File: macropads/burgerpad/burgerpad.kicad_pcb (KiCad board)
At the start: 2 copper layers, 1 part, among them U1 RP2040-ZERO

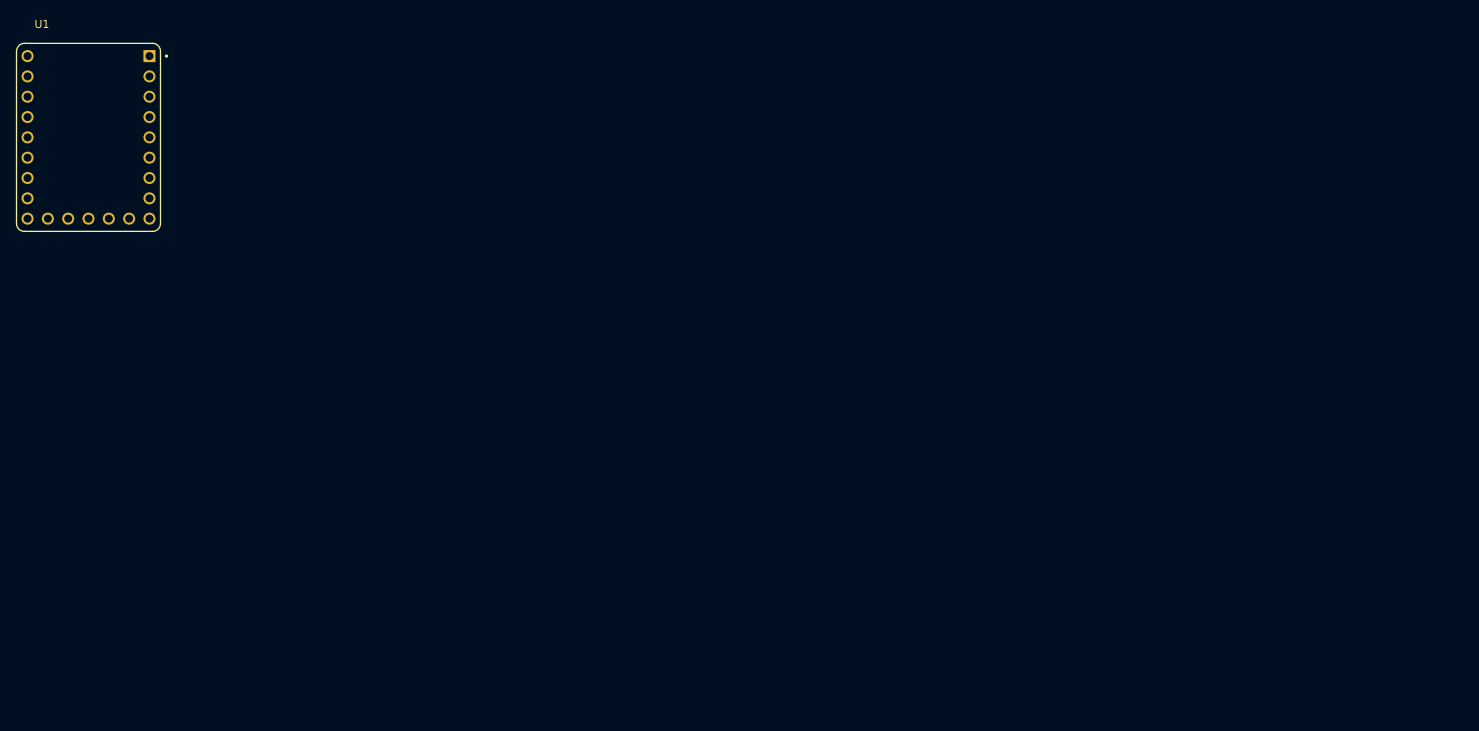
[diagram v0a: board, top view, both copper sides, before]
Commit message: Made schematic and did PCB layouts
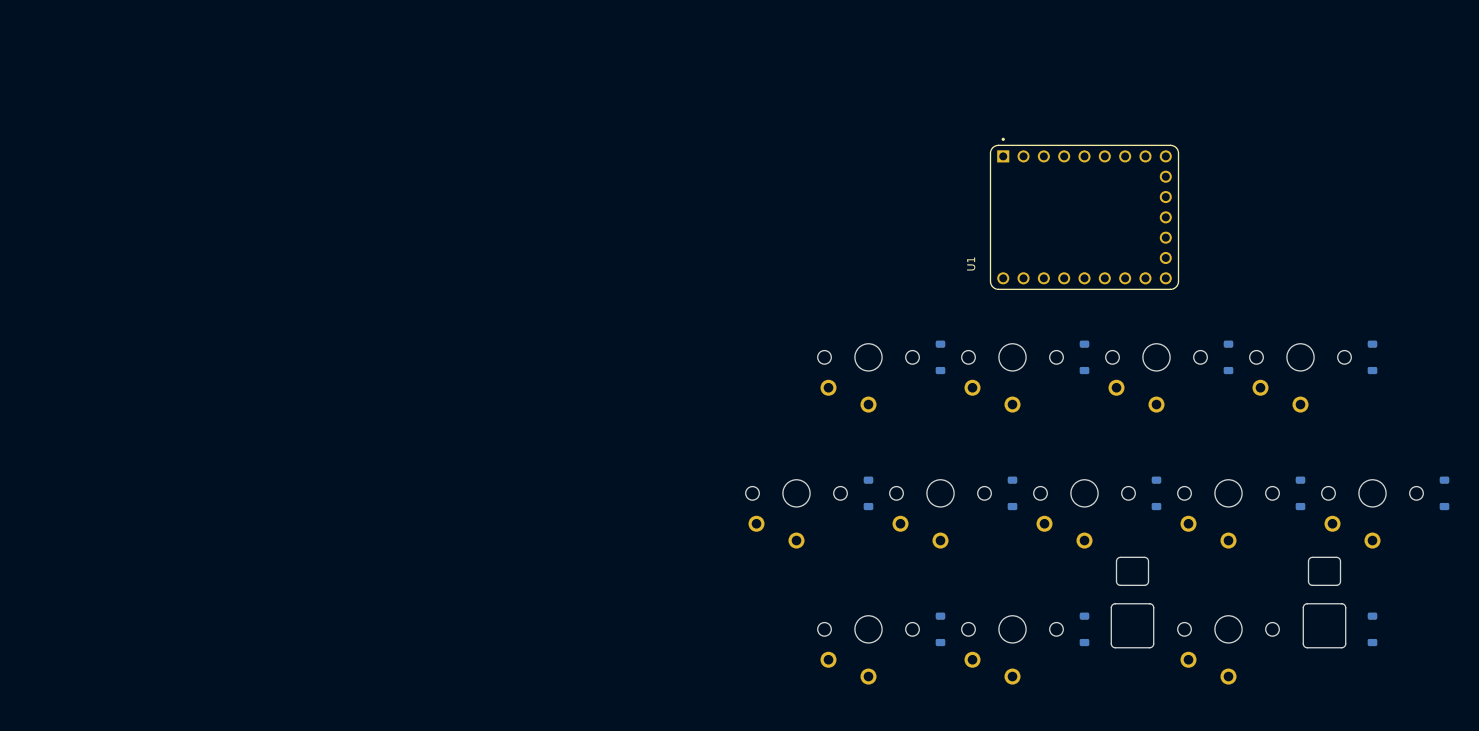
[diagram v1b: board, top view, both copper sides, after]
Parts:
- added CH1: choc_v1_SW_solder, PCM_marbastlib-choc:SW_choc_v1_1u, F.Cu at (143.0, 76.5)
- added CH10: choc_v1_SW_solder, PCM_marbastlib-choc:SW_choc_v1_1u, F.Cu at (197.0, 76.5)
- added CH11: choc_v1_SW_solder, PCM_marbastlib-choc:SW_choc_v1_1u, F.Cu at (188.0, 93.5)
- added CH12: choc_v1_SW_solder, PCM_marbastlib-choc:SW_choc_v1_1u, F.Cu at (206.0, 93.5)
- added CH2: choc_v1_SW_solder, PCM_marbastlib-choc:SW_choc_v1_1u, F.Cu at (134.0, 93.5)
- added CH3: choc_v1_SW_solder, PCM_marbastlib-choc:SW_choc_v1_1u, F.Cu at (143.0, 110.5)
- added CH4: choc_v1_SW_solder, PCM_marbastlib-choc:SW_choc_v1_1u, F.Cu at (161.0, 76.5)
- added CH5: choc_v1_SW_solder, PCM_marbastlib-choc:SW_choc_v1_1u, F.Cu at (152.0, 93.5)
- added CH6: choc_v1_SW_solder, PCM_marbastlib-choc:SW_choc_v1_1u, F.Cu at (161.0, 110.5)
- added CH7: choc_v1_SW_solder, PCM_marbastlib-choc:SW_choc_v1_1u, F.Cu at (179.0, 76.5)
- added CH8: choc_v1_SW_solder, PCM_marbastlib-choc:SW_choc_v1_1u, F.Cu at (170.0, 93.5)
- added CH9: choc_v1_SW_solder, PCM_marbastlib-choc:SW_choc_v1_1u, F.Cu at (188.0, 110.5)
- added D13: 1N4148W, Diode_SMD:D_SOD-123, B.Cu at (152.0, 76.5)
- added D14: 1N4148W, Diode_SMD:D_SOD-123, B.Cu at (170.0, 76.5)
- added D15: 1N4148W, Diode_SMD:D_SOD-123, B.Cu at (188.0, 76.5)
- added D16: 1N4148W, Diode_SMD:D_SOD-123, B.Cu at (206.0, 76.5)
- added D17: 1N4148W, Diode_SMD:D_SOD-123, B.Cu at (143.0, 93.5)
- added D18: 1N4148W, Diode_SMD:D_SOD-123, B.Cu at (161.0, 93.5)
- added D19: 1N4148W, Diode_SMD:D_SOD-123, B.Cu at (179.0, 93.5)
- added D20: 1N4148W, Diode_SMD:D_SOD-123, B.Cu at (197.0, 93.5)
- added D21: 1N4148W, Diode_SMD:D_SOD-123, B.Cu at (152.0, 110.5)
- added D22: 1N4148W, Diode_SMD:D_SOD-123, B.Cu at (170.0, 110.5)
- added D23: 1N4148W, Diode_SMD:D_SOD-123, B.Cu at (206.0, 110.5)
- added D24: 1N4148W, Diode_SMD:D_SOD-123, B.Cu at (215.0, 93.5)
- added S1: choc_stab, PCM_marbastlib-xp-choc:STAB_choc_2u, F.Cu at (188.0, 110.5)
- moved U1 124.9 mm to (170.0, 59.0), turned to 90 degrees
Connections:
- U1 pad 1: unconnected-(U1-GP0-Pad1) -> Col 0
- U1 pad 11: unconnected-(U1-GP10-Pad11) -> Row 0
- U1 pad 12: unconnected-(U1-GP11-Pad12) -> Row 1
- U1 pad 13: unconnected-(U1-GP12-Pad13) -> Row 2
- U1 pad 2: unconnected-(U1-GP1-Pad2) -> Col 1
- U1 pad 22: unconnected-(U1-GND-Pad22) -> GND
- U1 pad 3: unconnected-(U1-GP2-Pad3) -> Col 2
- U1 pad 4: unconnected-(U1-GP3-Pad4) -> Col 3
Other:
- board outline added: 29.3 x 11.3 mm

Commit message: burgerpad borderpad
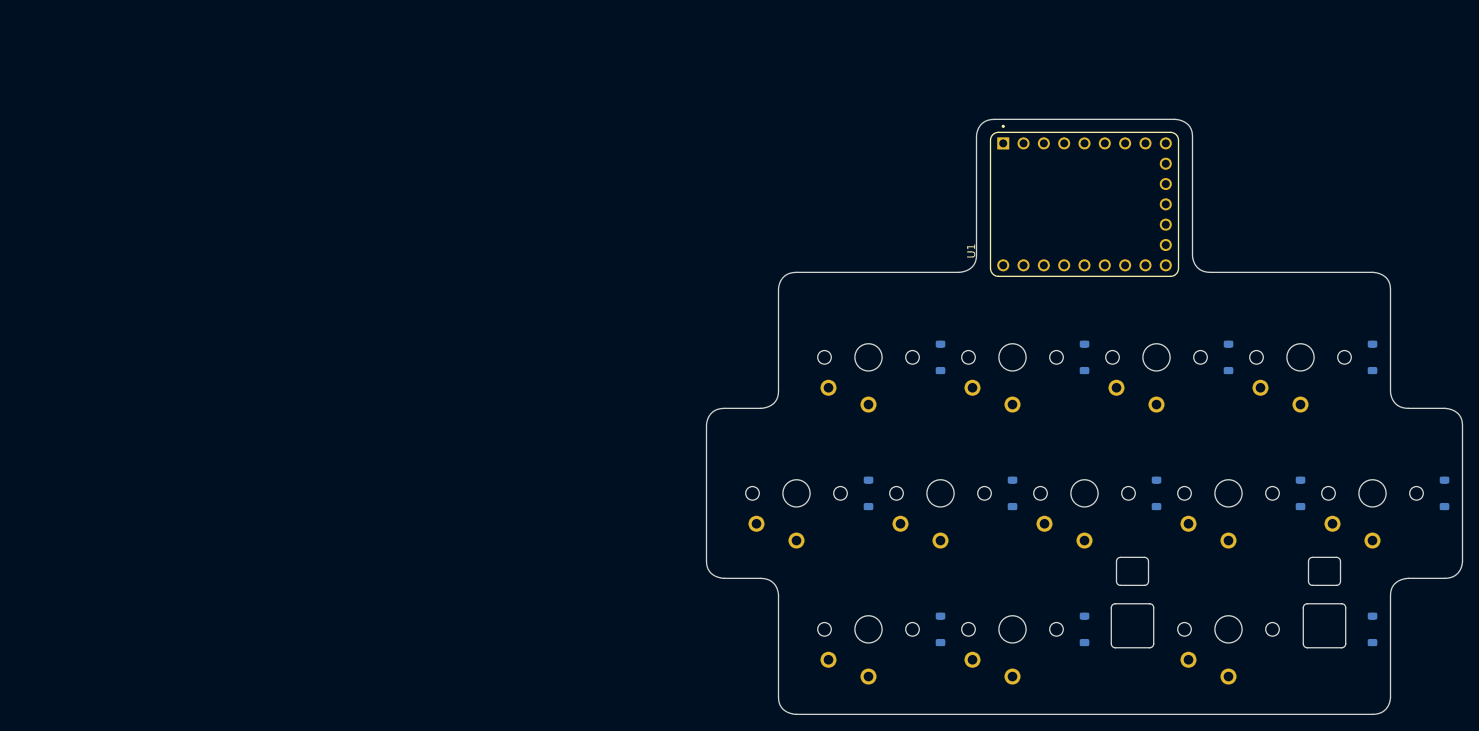
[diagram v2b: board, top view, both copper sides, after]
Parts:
- moved U1 1.62 mm to (170.0, 57.4)
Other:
- board size 29.3 x 11.3 mm -> 94.5 x 74.4 mm

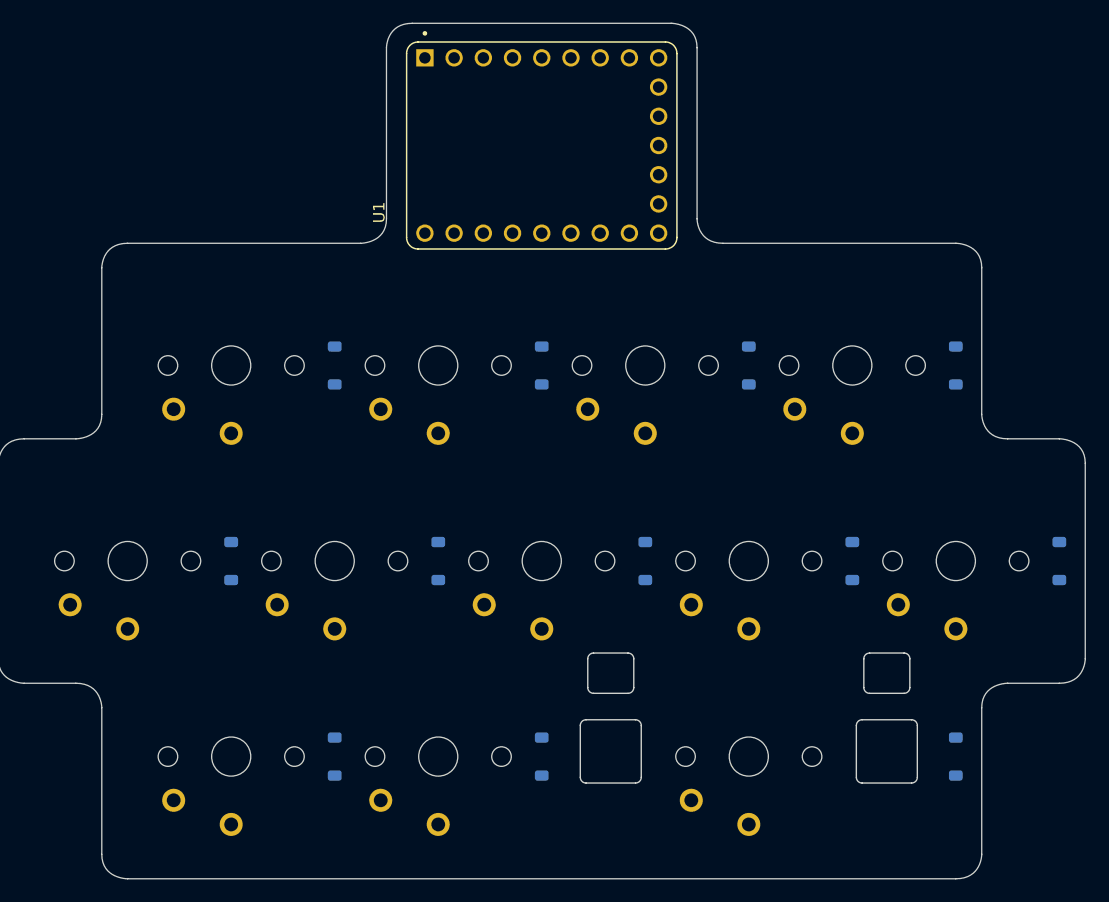
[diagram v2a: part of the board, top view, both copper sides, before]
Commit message: Added traces and ran DRC on PCB
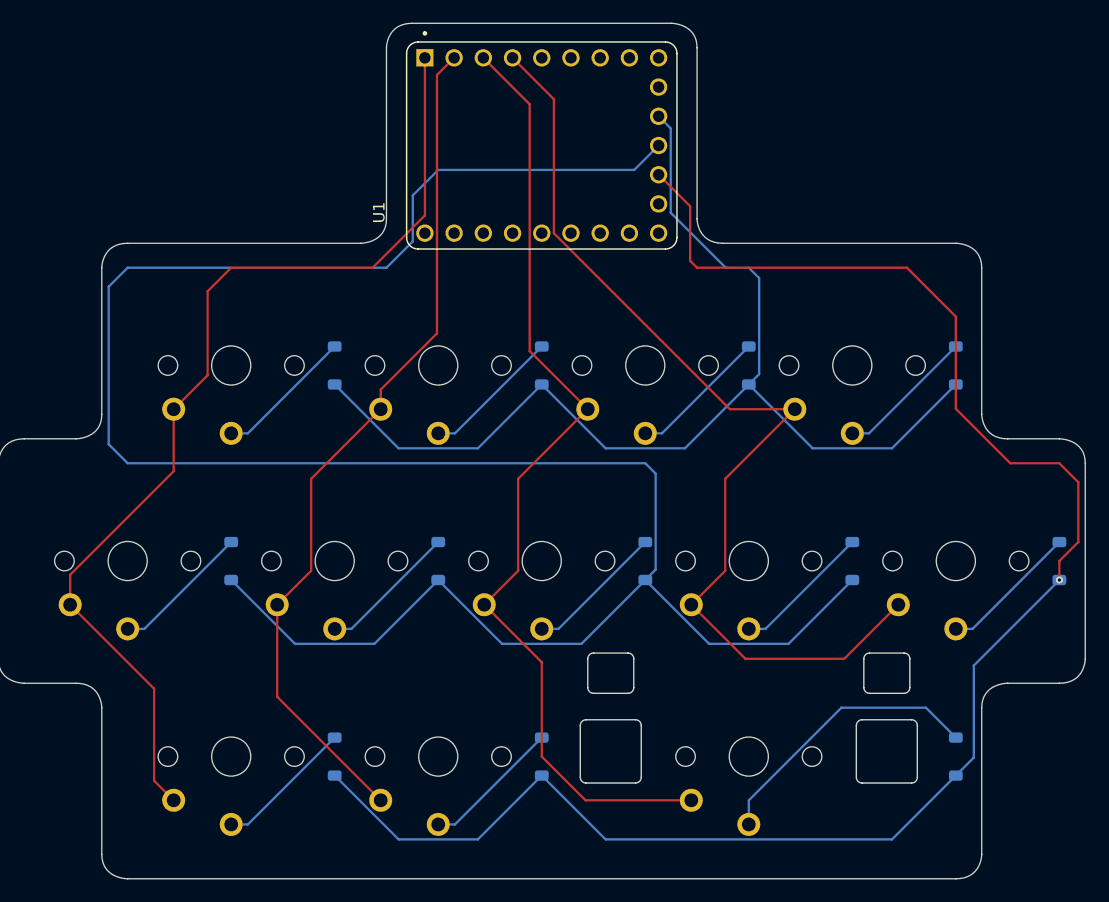
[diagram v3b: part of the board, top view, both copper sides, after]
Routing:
- net Row 1: track 0.00 -> 195.0 mm
- net Row 2: track 0.00 -> 148.1 mm, vias 0 -> 1
- net Row 0: track 0.00 -> 96.3 mm
- net Col 0: track 0.00 -> 88.9 mm
- net Col 3: track 0.00 -> 86.6 mm
- net Col 2: track 0.00 -> 84.9 mm
- net Col 1: track 0.00 -> 74.6 mm
- net Net-(D23-A): track 0.00 -> 24.5 mm
- net Net-(D24-A): track 0.00 -> 12.1 mm
- net Net-(D22-A): track 0.00 -> 12.1 mm
- net Net-(D21-A): track 0.00 -> 12.1 mm
- net Net-(D20-A): track 0.00 -> 12.1 mm
- net Net-(D19-A): track 0.00 -> 12.1 mm
- net Net-(D18-A): track 0.00 -> 12.1 mm
- net Net-(D17-A): track 0.00 -> 12.1 mm
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
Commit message: Updated schematic and PCB to match new layout
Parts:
- removed S1: choc_stab, PCM_marbastlib-xp-choc:STAB_choc_2u
- added CH13: choc_v1_SW_solder, PCM_marbastlib-choc:SW_choc_v1_1u, F.Cu at (197.0, 110.5)
- added D25: 1N4148W, Diode_SMD:D_SOD-123, B.Cu at (206.0, 110.5)
- moved D23 18.0 mm to (188.0, 110.5)
- moved CH9 9.00 mm to (179.0, 110.5)
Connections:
- U1 pad 14: unconnected-(U1-GP13-Pad14) -> Row 3
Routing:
- net Row 3: track 0.00 -> 81.3 mm, vias 0 -> 2
- net Col 3: track 86.6 -> 100.7 mm
- net Net-(D23-A): track 24.5 -> 12.1 mm
- net Net-(D25-A): track 0.00 -> 12.1 mm
- net Row 2: track 148.1 -> 157.7 mm
- net Col 2: track 84.9 -> 75.7 mm
